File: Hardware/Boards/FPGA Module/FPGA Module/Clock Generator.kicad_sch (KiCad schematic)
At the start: 31 parts, among them U21 Si5338A-B-GMR, Y2 12Mhz

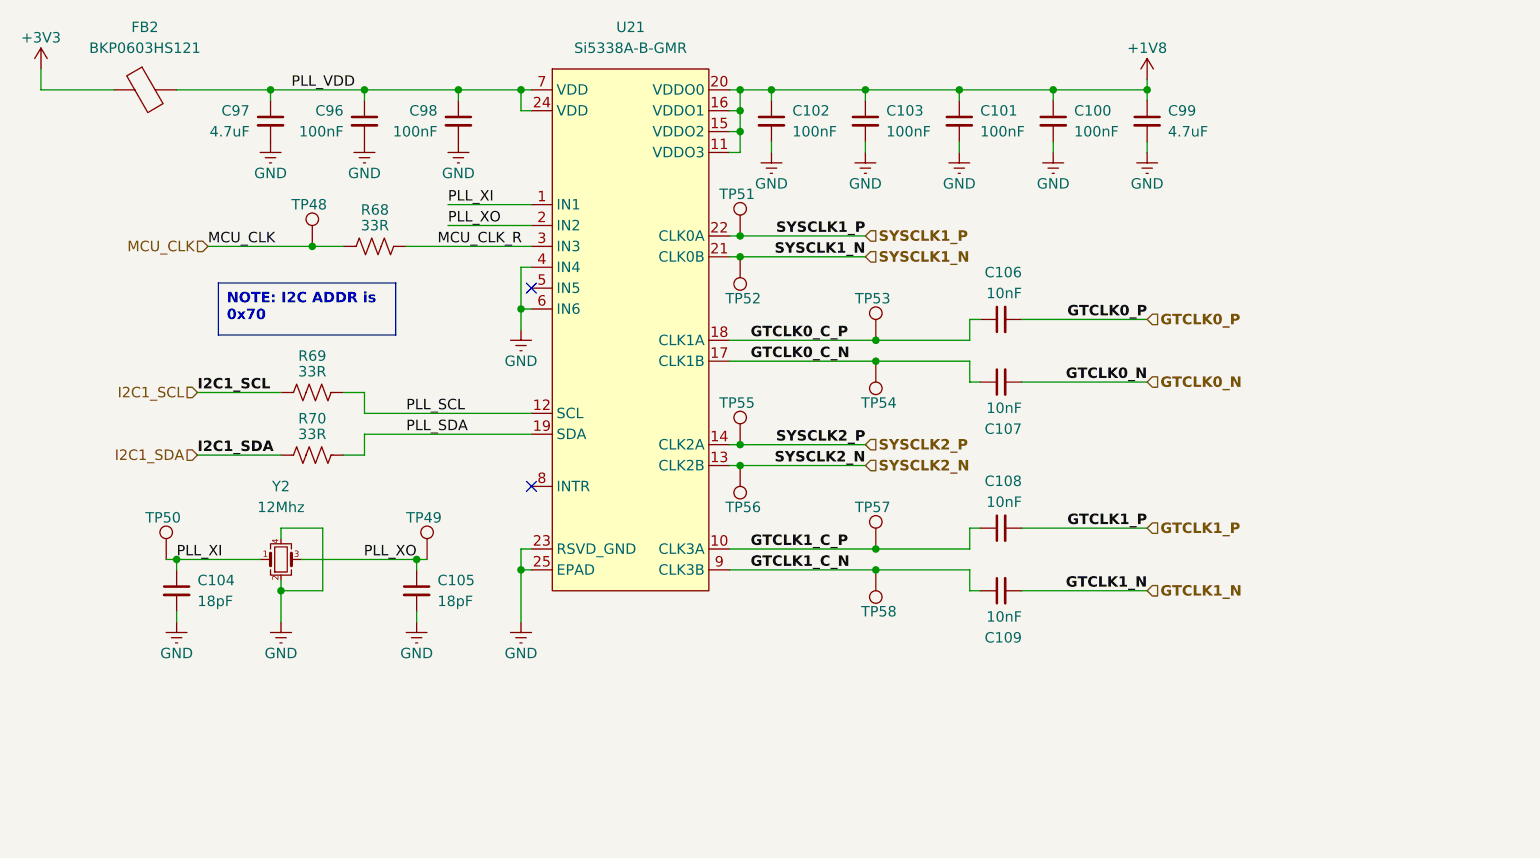
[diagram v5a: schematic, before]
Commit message: Completed FPGA module PCB layout
Started PCB routing
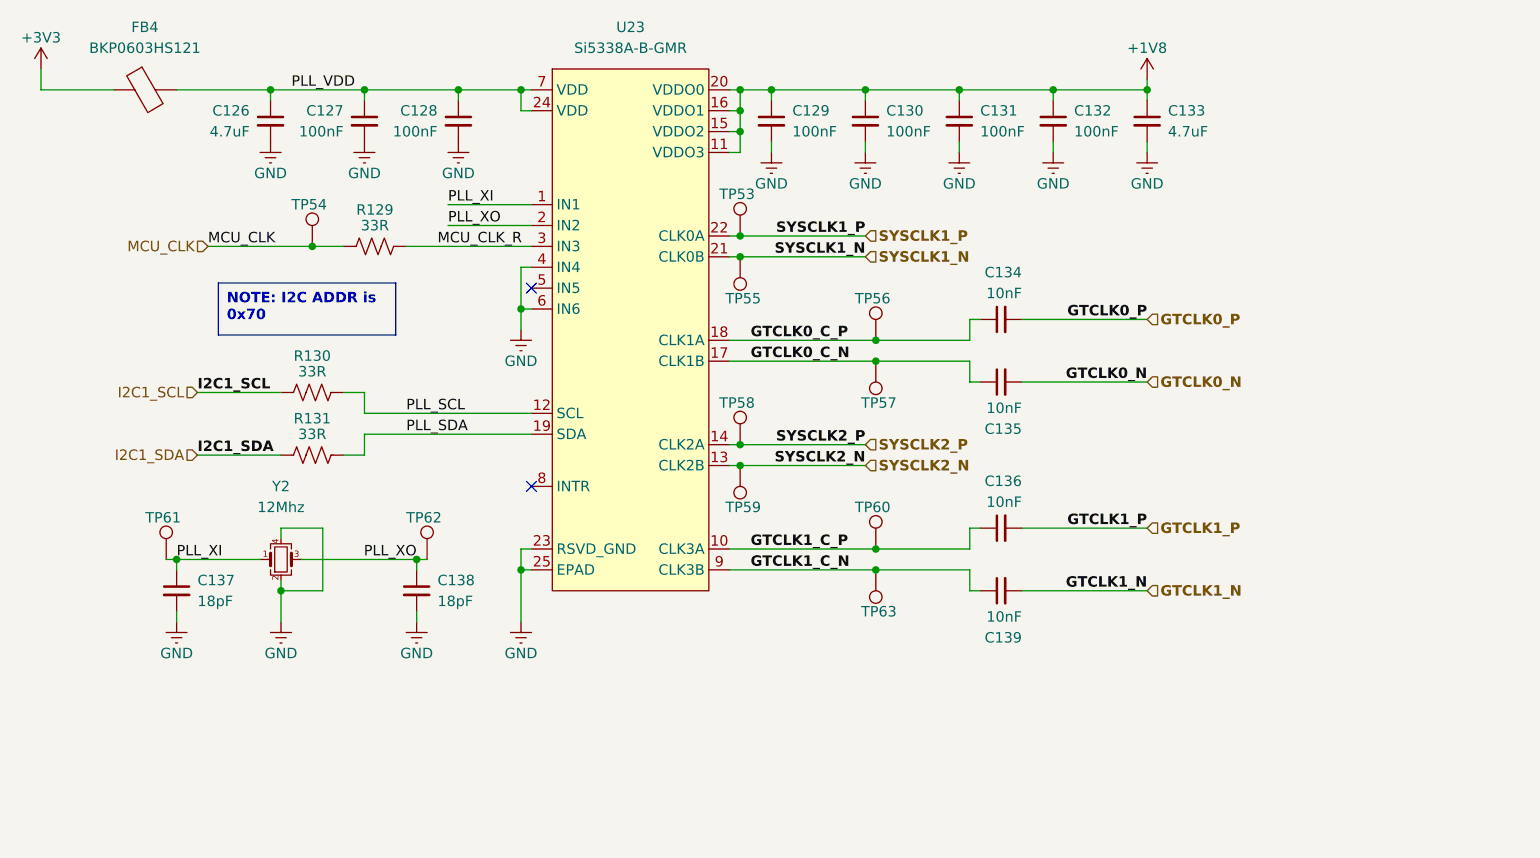
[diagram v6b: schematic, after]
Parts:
- C127: renamed from C96; footprint Capacitor_SMD:C_0402_1005Metric -> Capacitor_SMD:C_0201_0603Metric
- C128: renamed from C98; footprint Capacitor_SMD:C_0402_1005Metric -> Capacitor_SMD:C_0201_0603Metric
- C129: renamed from C102; footprint Capacitor_SMD:C_0402_1005Metric -> Capacitor_SMD:C_0201_0603Metric
- C130: renamed from C103; footprint Capacitor_SMD:C_0402_1005Metric -> Capacitor_SMD:C_0201_0603Metric
- C131: renamed from C101; footprint Capacitor_SMD:C_0402_1005Metric -> Capacitor_SMD:C_0201_0603Metric
- C132: renamed from C100; footprint Capacitor_SMD:C_0402_1005Metric -> Capacitor_SMD:C_0201_0603Metric
- C134: renamed from C106; footprint Capacitor_SMD:C_0402_1005Metric -> Capacitor_SMD:C_0201_0603Metric
- C135: renamed from C107; footprint Capacitor_SMD:C_0402_1005Metric -> Capacitor_SMD:C_0201_0603Metric
- C136: renamed from C108; footprint Capacitor_SMD:C_0402_1005Metric -> Capacitor_SMD:C_0201_0603Metric
- C139: renamed from C109; footprint Capacitor_SMD:C_0402_1005Metric -> Capacitor_SMD:C_0201_0603Metric
- FB4: renamed from FB2; footprint (none) -> Inductor_SMD:L_0201_0603Metric
- R129: renamed from R68; footprint Resistor_SMD:R_0402_1005Metric -> Resistor_SMD:R_0201_0603Metric
- R130: renamed from R69; footprint Resistor_SMD:R_0402_1005Metric -> Resistor_SMD:R_0201_0603Metric
- R131: renamed from R70; footprint Resistor_SMD:R_0402_1005Metric -> Resistor_SMD:R_0201_0603Metric
- renumbered C97 to C126, C99 to C133, C104 to C137, C105 to C138, TP51 to TP53, TP48 to TP54, TP52 to TP55, TP53 to TP56, TP54 to TP57, TP55 to TP58, TP56 to TP59, TP57 to TP60, TP50 to TP61, TP49 to TP62, TP58 to TP63, U21 to U23

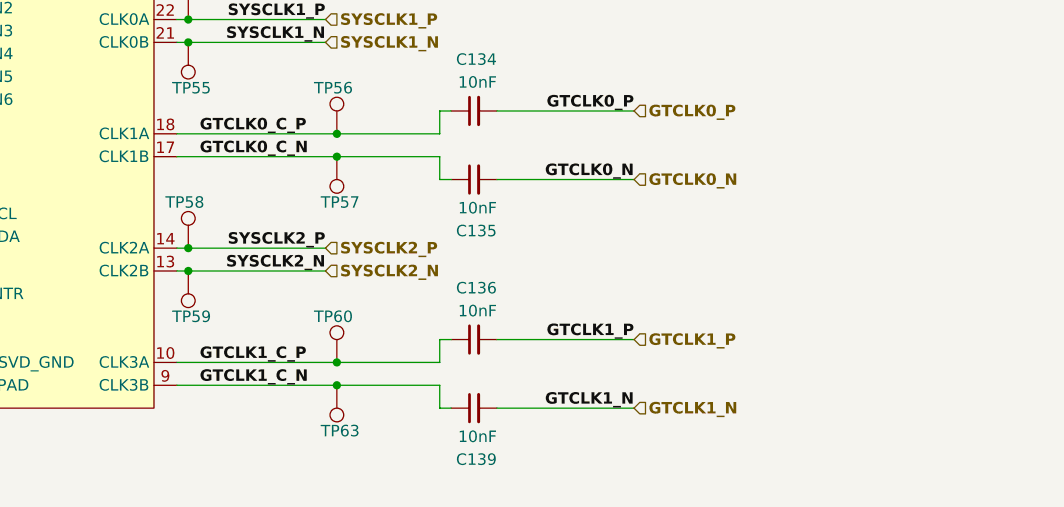
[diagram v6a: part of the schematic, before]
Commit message: Updated SCH and Layout
Added temp sensors for DCDC's, Added MCU control for FPGA mode, removed mode DIP switch
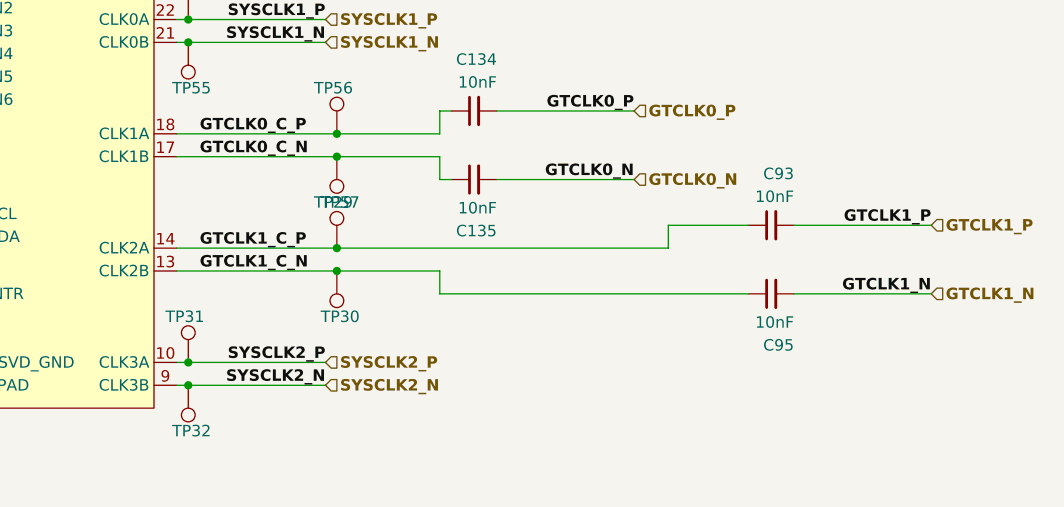
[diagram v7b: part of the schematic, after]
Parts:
- removed C136, C139: 10nF, Capacitor_SMD:C_0201_0603Metric, symbol Device:C_Small
- removed TP58, TP59, TP60, TP63: Test Point, FPGA Module:Test Point 0.75mm, symbol Connector:TestPoint
- added C93, C95: 10nF, Capacitor_SMD:C_0201_0603Metric, symbol Device:C_Small
- added TP29, TP30, TP31, TP32: Test Point, FPGA Module:Test Point 0.75mm, symbol Connector:TestPoint
- C126, C133: footprint Capacitor_SMD:C_0402_1005Metric -> Capacitor_SMD:C_0201_0603Metric
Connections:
- net GTCLK1_C_N: now also U23.13 (CLK2B), C95.1, TP30.1; no longer U23.9 (CLK3B)
- net GTCLK1_C_P: now also U23.14 (CLK2A), C93.1, TP29.1; no longer U23.10 (CLK3A)
- net GTCLK1_N: now also C95.2
- net GTCLK1_P: now also C93.2
- net SYSCLK2_N: now also U23.9 (CLK3B), TP32.1; no longer U23.13 (CLK2B)
- net SYSCLK2_P: now also U23.10 (CLK3A), TP31.1; no longer U23.14 (CLK2A)

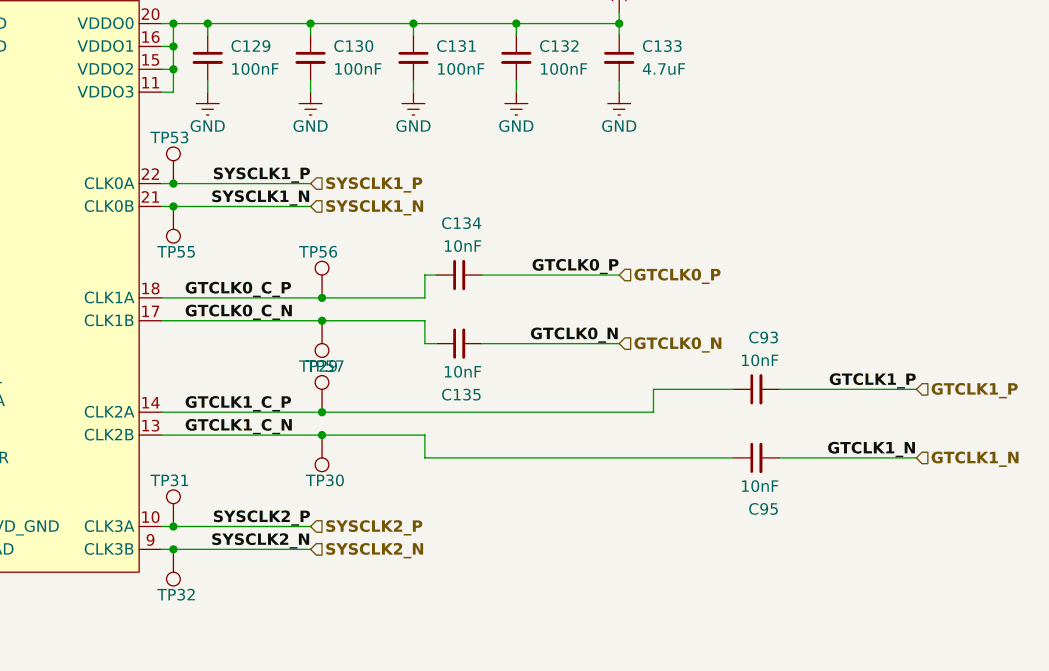
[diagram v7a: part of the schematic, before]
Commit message: Updated FPGA Module Routing
Cleaned up routing
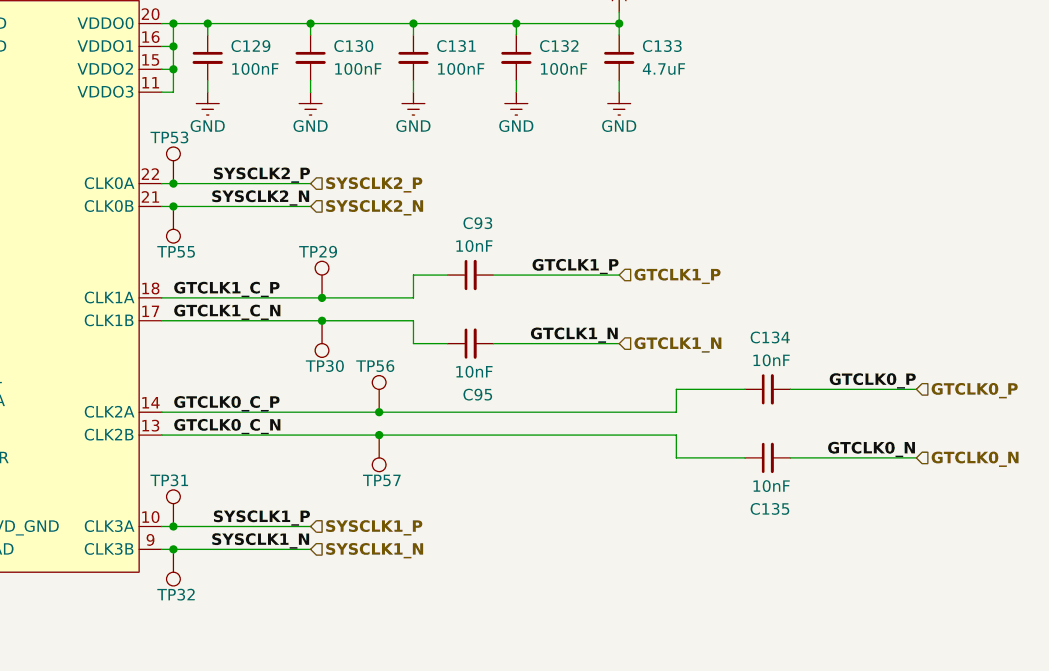
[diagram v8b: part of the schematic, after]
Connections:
- net GTCLK0_C_N: now also U23.13 (CLK2B); no longer U23.17 (CLK1B)
- net GTCLK0_C_P: now also U23.14 (CLK2A); no longer U23.18 (CLK1A)
- net GTCLK1_C_N: now also U23.17 (CLK1B); no longer U23.13 (CLK2B)
- net GTCLK1_C_P: now also U23.18 (CLK1A); no longer U23.14 (CLK2A)
- net SYSCLK1_N: now also TP32.1, U23.9 (CLK3B); no longer TP55.1, U23.21 (CLK0B)
- net SYSCLK1_P: now also TP31.1, U23.10 (CLK3A); no longer TP53.1, U23.22 (CLK0A)
- net SYSCLK2_N: now also TP55.1, U23.21 (CLK0B); no longer TP32.1, U23.9 (CLK3B)
- net SYSCLK2_P: now also TP53.1, U23.22 (CLK0A); no longer TP31.1, U23.10 (CLK3A)
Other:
- moved on the sheet: C134, C135, C93, C95, TP29, TP30, TP56, TP57
